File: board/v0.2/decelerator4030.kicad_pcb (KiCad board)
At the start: 2 copper layers, 174 parts, among them CON1 A3000/A4000_LOCAL_BUS_SLOT, J3 XILINX_JTAG, J4 CONN_2, J5 CONN_4, U1 MC68030FE, U10 74LXC245, U11 74LXC245, U12 MCP9801, U13 DS1086L, U14 XTAL_OSC_DIP8, U15 MCP1826S, U16 IS66WVE4M16, U17 IS66WVE4M16, U18 MC68030RC_PGA, U19 XC9536XL-5VQG44C, U2 XC95144XL-10TQG144C, U20 MCP9801, U3 AS6C3216, U4 AS6C3216, U5 S29AL016J, U6 S29AL016J, U7 PCA9564, U8 74LXC245, U9 74LXC245

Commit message: Litle change of board
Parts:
- added ?: , LOGO, F.Cu at (77.3, 41.8)
- ? (x89): footprint PINTST_0.5 -> PINTST_0.8
- J5: value CONN_4 -> I2C_EXT
- moved ? 4.14 mm to (193.5, 62.8)
- moved ? 1.22 mm to (224.7, 45.0)
- moved ? 1.14 mm to (222.9, 63.1)
- moved ? 1.07 mm to (222.1, 55.2)
- moved ? 1.03 mm to (225.1, 43.5)
- moved ? 1.02 mm to (222.3, 57.7)
- moved ? 0.90 mm to (83.6, 80.0)
- moved ? 0.75 mm to (56.6, 85.9)
- moved ? 0.60 mm to (224.4, 41.8)
- moved ? 0.45 mm to (223.4, 42.9)
- moved C27 0.42 mm to (45.0, 63.6)
- moved ? 0.41 mm to (55.9, 88.1)
- moved ? 0.33 mm to (172.3, 80.9)
- moved ? 0.31 mm to (82.6, 76.1)
- moved ? 0.28 mm to (222.5, 43.9)
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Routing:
- net GND: track 695.8 -> 730.1 mm, vias 112 -> 120
- net +5V: track 664.3 -> 683.0 mm, vias 6 -> 8
- net (no net): track 16.7 -> 11.4 mm, vias 4 -> 2
- net /ARM12: track 130.1 -> 128.0 mm
- net /ARM13: track 123.5 -> 121.9 mm
- net /ARM9: track 130.2 -> 131.7 mm
- net /ARM2: track 189.1 -> 190.2 mm
- net /ARM4: track 177.1 -> 178.2 mm
- net /ARM5: track 168.8 -> 169.7 mm
- net /ARM6: track 167.2 -> 168.0 mm
- net /ARM7: track 163.2 -> 164.0 mm
- net /ARM17: track 156.9 -> 157.7 mm
- net /ARM18: track 157.9 -> 158.8 mm
- net /ARM11: track 125.1 -> 125.9 mm
- net /ARM19: track 146.1 -> 147.0 mm
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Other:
- board text added: "Decelerator 4030 Proto v0.2"
- board text removed: "Decelerator 4030 Proto v1.0"
- board text removed: "SAKURA"

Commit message: Finaly proto goard
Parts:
- moved Hole_4mm 4.01 mm to (207.5, 32.3)
- moved Hole_4mm 3.75 mm to (42.0, 32.3)
- moved Hole_4mm 0.65 mm to (42.0, 101.0)
- moved Hole_4mm 0.42 mm to (207.5, 101.0)
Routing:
- net GND: track 730.1 -> 764.6 mm, vias 120 -> 127
- net +5V: track 683.0 -> 712.8 mm
- net (no net): track 11.4 -> 4.44 mm, vias 2 -> 1
- net SIZ1: track 141.4 -> 142.0 mm

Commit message: Removing errors in board
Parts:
- added D4: 1N4148, SM1206POL, F.Cu at (146.3, 104.2)
- J5: value I2C_EXT -> CONN_4
- U12: footprint MSOP_8 -> MSOP-8
- U15: footprint DPAK3 -> D2PAK3
- U18: footprint MC68030RC_PGA -> MC68030
- moved U15 15.9 mm to (213.0, 85.7), turned to 90 degrees
- moved C7 11.7 mm to (218.9, 82.4), turned to 90 degrees
- moved C20 7.34 mm to (218.8, 88.8), turned to 270 degrees
- moved ? 5.27 mm to (188.5, 61.0)
- moved ? 3.43 mm to (214.5, 39.6)
- moved ? 3.43 mm to (192.4, 62.1)
- moved ? 3.43 mm to (197.2, 56.6)
- moved ? 3.43 mm to (206.3, 56.6)
- moved ? 3.43 mm to (194.8, 39.9)
- moved ? 3.43 mm to (192.5, 38.3)
- moved ? 3.43 mm to (192.6, 41.9)
- moved ? 3.43 mm to (216.8, 54.2)
- moved ? 3.43 mm to (214.6, 55.5)
- moved ? 3.43 mm to (218.9, 57.7)
- moved ? 3.43 mm to (212.6, 56.6)
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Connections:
- CON1 pad 134: (no net) -> _FPUCS
- U1 pad 119: SIZ0 -> SIZ1
- U1 pad 120: SIZ1 -> SIZ0
- U2 pad 26: (no net) -> _CIIN
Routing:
- net _BERR: track 117.8 -> 186.0 mm, vias 3 -> 4
- net _CIIN: track 153.0 -> 215.0 mm, vias 3 -> 5
- net GND: track 764.6 -> 753.4 mm, vias 127 -> 131
- net +3.3V: track 812.4 -> 802.5 mm
- net _INT2: track 58.4 -> 50.6 mm
- net _DSACK0: track 109.8 -> 117.3 mm
- net CPUCLK_EXP: track 94.9 -> 102.0 mm
- net _EMUL: track 131.0 -> 137.8 mm, vias 2 -> 3
- net +5V: track 712.8 -> 706.3 mm
- net _WAIT: track 60.3 -> 66.4 mm, vias 2 -> 3
- net _FPUCS: track 0.00 -> 3.93 mm
- net _SRAM_WE: track 117.9 -> 114.4 mm
- net /ARM11: track 125.9 -> 122.5 mm
- net /ARM0: track 165.3 -> 161.8 mm
- net /ARM18: track 158.8 -> 155.3 mm
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
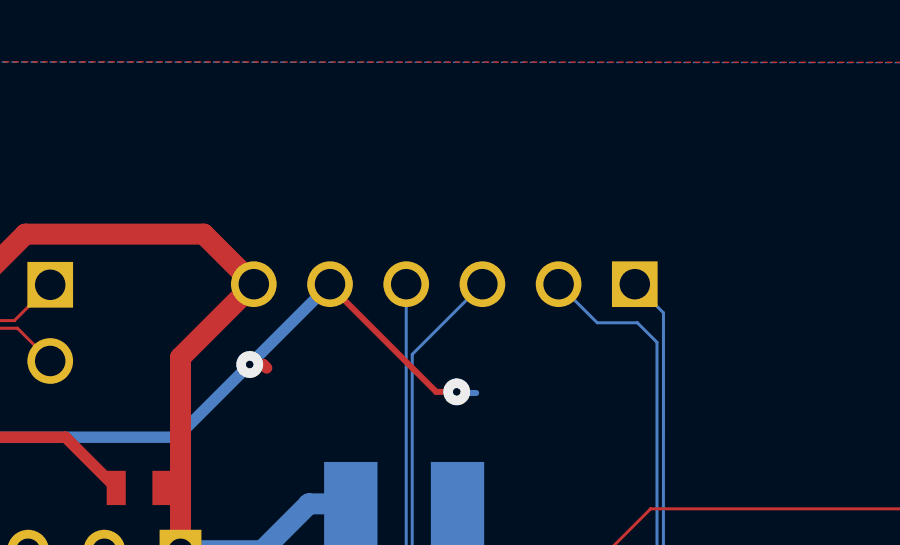
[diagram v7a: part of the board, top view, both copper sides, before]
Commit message: Add pull up resistors and _CIIN to CPLD
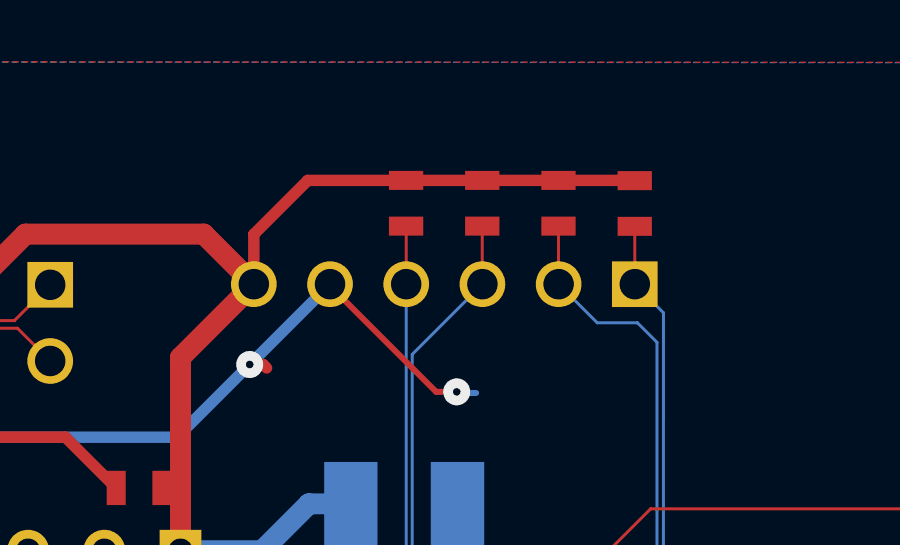
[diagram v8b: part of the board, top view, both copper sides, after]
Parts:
- added R10: 4k7, SM0603, F.Cu at (147.7, 27.8)
- added R11: 4k7, SM0603, F.Cu at (155.3, 27.8)
- added R12: 4k7, SM0603, F.Cu at (150.2, 27.8)
- added R9: 4k7, SM0603, F.Cu at (152.8, 27.8)
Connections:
- net N-00000144 renamed TDI
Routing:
- net +3.3V: track 802.5 -> 817.6 mm
- net TDI: track 66.9 -> 68.9 mm
- net TDO2: track 178.9 -> 180.9 mm
- net TCK: track 164.7 -> 166.7 mm
- net TMS: track 160.6 -> 162.5 mm
